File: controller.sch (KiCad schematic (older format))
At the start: 29 parts, among them Q1 Q_PMOS_SGD, Q2 Q_PMOS_SGD, SW1 L1, SW2 L2, SW3 Select, SW4 Start, SW5 R2, SW6 R1, U4 dpad-cross-trace, U5 ProMicro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

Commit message: Add SMD dome switch footprint.
Link diode, dome switch, and pro micro footprints to their symbols. Add
the pro micro subdirectory footprint library to the library list.
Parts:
- D1, D10, D11, D12, D13, D14, D15, D16, D2, D3, D4, D5, D6, D7, D8, D9: footprint (none) -> Diode_THT:D_DO-35_SOD27_P7.62mm_Horizontal
- SW3, SW4: footprint (none) -> rpi-shell-v1-switches:SW_SMD_Dome_TL3312NF-160Q
- U5: footprint (none) -> kicad-pro-micro:ProMicro
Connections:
- wire segments 109 -> 97
- no-connect marks 10 -> 22
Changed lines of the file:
@@
 F 0 "D1" V 2004 1730 50  0000 L CNN
 F 1 "D_Schottky" V 2095 1730 50  0000 L CNN
-F 2 "" H 2050 1650 50  0001 C CNN
+F 2 "Diode_THT:D_DO-35_SOD27_P7.62mm_Horizontal" H 2050 1650 50  0001 C CNN
 F 3 "~" H 2050 1650 50  0001 C CNN
 	1    2050 1650
@@
 F 0 "SW3" H 3500 1585 50  0000 C CNN
 F 1 "Select" H 3500 1494 50  0000 C CNN
-F 2 "" H 3500 1500 50  0001 C CNN
+F 2 "rpi-shell-v1-switches:SW_SMD_Dome_TL3312NF-160Q" H 3500 1500 50  0001 C CNN
 F 3 "http://www.apem.com/int/index.php?controller=attachment&id_attachment=1371" H 3500 1500 50  0001 C CNN
 	1    3500 1200
@@
 F 0 "SW4" H 8150 1685 50  0000 C CNN
 F 1 "Start" H 8150 1594 50  0000 C CNN
-F 2 "" H 8150 1600 50  0001 C CNN
+F 2 "rpi-shell-v1-switches:SW_SMD_Dome_TL3312NF-160Q" H 8150 1600 50  0001 C CNN
 F 3 "http://www.apem.com/int/index.php?controller=attachment&id_attachment=1371" H 8150 1600 50  0001 C CNN
 	1    8150 1300
@@
 F 0 "U5" H 5850 4887 60  0000 C CNN
 F 1 "ProMicro" H 5850 4781 60  0000 C CNN
-F 2 "" H 5950 2800 60  0000 C CNN
+F 2 "kicad-pro-micro:ProMicro" H 5950 2800 60  0001 C CNN
 F 3 "" H 5950 2800 60  0000 C CNN
 	1    5850 3850
@@
 	1500 1200 1500 1350
 Wire Wire Line
-	1650 1100 1650 1200
-Connection ~ 1650 1200
-Wire Wire Line
-	2500 1100 2500 1200
-Wire Wire Line
 	2500 1200 2500 1350
 Wire Wire Line
 	2500 1350 1500 1350
-Connection ~ 2500 1200
-Wire Wire Line
-	3300 1100 3300 1200
 Wire Wire Line
 	3300 1200 3300 1350
 Wire Wire Line
 	3300 1350 2500 1350
-Connection ~ 3300 1200
 Connection ~ 2500 1350
-Wire Wire Line
-	3700 1100 3700 1200
-Wire Wire Line
-	2900 1100 2900 1200
-Wire Wire Line
-	2050 1100 2050 1200
 $Comp
 L Device:D_Schottky D2
@@
 F 0 "D2" V 2854 1730 50  0000 L CNN
 F 1 "D_Schottky" V 2945 1730 50  0000 L CNN
-F 2 "" H 2900 1650 50  0001 C CNN
+F 2 "Diode_THT:D_DO-35_SOD27_P7.62mm_Horizontal" H 2900 1650 50  0001 C CNN
 F 3 "~" H 2900 1650 50  0001 C CNN
 	1    2900 1650
@@
 F 0 "D3" V 3654 1730 50  0000 L CNN
 F 1 "D_Schottky" V 3745 1730 50  0000 L CNN
-F 2 "" H 3700 1650 50  0001 C CNN
+F 2 "Diode_THT:D_DO-35_SOD27_P7.62mm_Horizontal" H 3700 1650 50  0001 C CNN
 F 3 "~" H 3700 1650 50  0001 C CNN
 	1    3700 1650
@@
 Wire Wire Line
 	3700 1200 3700 1500
-Connection ~ 3700 1200
 Wire Wire Line
 	2900 1200 2900 1500
-Connection ~ 2900 1200
 Wire Wire Line
 	2050 1200 2050 1500
-Connection ~ 2050 1200
 Wire Wire Line
 	3300 1350 4300 1350
@@
 F 0 "D14" V 7904 1730 50  0000 L CNN
 F 1 "D_Schottky" V 7995 1730 50  0000 L CNN
-F 2 "" H 7950 1650 50  0001 C CNN
+F 2 "Diode_THT:D_DO-35_SOD27_P7.62mm_Horizontal" H 7950 1650 50  0001 C CNN
 F 3 "~" H 7950 1650 50  0001 C CNN
 	1    7950 1650
@@
 F 0 "D15" V 8654 1730 50  0000 L CNN
 F 1 "D_Schottky" V 8745 1730 50  0000 L CNN
-F 2 "" H 8700 1650 50  0001 C CNN
+F 2 "Diode_THT:D_DO-35_SOD27_P7.62mm_Horizontal" H 8700 1650 50  0001 C CNN
 F 3 "~" H 8700 1650 50  0001 C CNN
 	1    8700 1650
@@
 F 0 "D16" V 9404 1730 50  0000 L CNN
 F 1 "D_Schottky" V 9495 1730 50  0000 L CNN
-F 2 "" H 9450 1650 50  0001 C CNN
+F 2 "Diode_THT:D_DO-35_SOD27_P7.62mm_Horizontal" H 9450 1650 50  0001 C CNN
 F 3 "~" H 9450 1650 50  0001 C CNN
 	1    9450 1650
@@
 $EndComp
 Wire Wire Line
-	7950 1200 7950 1300
-Wire Wire Line
 	7950 1300 7950 1500
-Connection ~ 7950 1300
 Wire Wire Line
 	8700 1300 8700 1500
 Wire Wire Line
-	8700 1200 8700 1300
-Connection ~ 8700 1300
-Wire Wire Line
-	9450 1200 9450 1300
-Wire Wire Line
-	9450 1300 9450 1500
-Connection ~ 9450 1300
-Wire Wire Line
 	7750 4100 6550 4100
 Wire Wire Line
@@
 	7750 3750 7450 3750
 Wire Wire Line
-	9850 1400 9850 1300
-Wire Wire Line
-	9850 1200 9850 1300
-Connection ~ 9850 1300
-Wire Wire Line
-	9100 1200 9100 1300
-Wire Wire Line
 	9100 1300 9100 1400
-Connection ~ 9100 1300
 Connection ~ 9100 1400
 Wire Wire Line
 	9100 1400 9850 1400
 Wire Wire Line
-	8350 1200 8350 1300
-Wire Wire Line
 	8350 1300 8350 1400
-Connection ~ 8350 1300
 Connection ~ 8350 1400
 Wire Wire Line
@@
 Wire Wire Line
 	4300 3600 4000 3600
-$Comp
-L Switch:SW_MEC_5E SW6
-U 1 1 60680BB6
-P 9650 1300
-F 0 "SW6" H 9650 1685 50  0000 C CNN
-F 1 "R1" H 9650 1594 50  0000 C CNN
-F 2 "" H 9650 1600 50  0001 C CNN
-F 3 "http://www.apem.com/int/index.php?controller=attachment&id_attachment=1371" H 9650 1600 50  0001 C CNN
-	1    9650 1300
-	1    0    0    -1
-$EndComp
 Wire Wire Line
 	3650 4400 6800 4400
@@
 F 0 "D4" V 4046 3170 50  0000 R CNN
 F 1 "D_Schottky" V 3955 3170 50  0000 R CNN
-F 2 "" H 4000 3250 50  0001 C CNN
+F 2 "Diode_THT:D_DO-35_SOD27_P7.62mm_Horizontal" H 4000 3250 50  0001 C CNN
 F 3 "~" H 4000 3250 50  0001 C CNN
 	1    4000 3250
@@
 F 0 "D13" V 7796 3420 50  0000 R CNN
 F 1 "D_Schottky" V 7705 3420 50  0000 R CNN
-F 2 "" H 7750 3500 50  0001 C CNN
+F 2 "Diode_THT:D_DO-35_SOD27_P7.62mm_Horizontal" H 7750 3500 50  0001 C CNN
 F 3 "~" H 7750 3500 50  0001 C CNN
 	1    7750 3500
@@
 F 0 "D10" H 6750 4933 50  0000 C CNN
 F 1 "D_Schottky" H 6750 5024 50  0000 C CNN
-F 2 "" H 6750 5150 50  0001 C CNN
+F 2 "Diode_THT:D_DO-35_SOD27_P7.62mm_Horizontal" H 6750 5150 50  0001 C CNN
 F 3 "~" H 6750 5150 50  0001 C CNN
 	1    6750 5150
@@
 F 0 "D11" H 6750 5633 50  0000 C CNN
 F 1 "D_Schottky" H 6750 5724 50  0000 C CNN
-F 2 "" H 6750 5850 50  0001 C CNN
+F 2 "Diode_THT:D_DO-35_SOD27_P7.62mm_Horizontal" H 6750 5850 50  0001 C CNN
 F 3 "~" H 6750 5850 50  0001 C CNN
 	1    6750 5850
@@
 F 0 "D12" H 6750 5933 50  0000 C CNN
 F 1 "D_Schottky" H 6750 6024 50  0000 C CNN
-F 2 "" H 6750 6150 50  0001 C CNN
+F 2 "Diode_THT:D_DO-35_SOD27_P7.62mm_Horizontal" H 6750 6150 50  0001 C CNN
 F 3 "~" H 6750 6150 50  0001 C CNN
 	1    6750 6150
@@
 F 0 "D5" H 4650 5217 50  0000 C CNN
 F 1 "D_Schottky" H 4650 5126 50  0000 C CNN
-F 2 "" H 4650 5000 50  0001 C CNN
+F 2 "Diode_THT:D_DO-35_SOD27_P7.62mm_Horizontal" H 4650 5000 50  0001 C CNN
 F 3 "~" H 4650 5000 50  0001 C CNN
 	1    4650 5000
@@
 F 0 "D6" H 4650 5467 50  0000 C CNN
 F 1 "D_Schottky" H 4650 5376 50  0000 C CNN
-F 2 "" H 4650 5250 50  0001 C CNN
+F 2 "Diode_THT:D_DO-35_SOD27_P7.62mm_Horizontal" H 4650 5250 50  0001 C CNN
 F 3 "~" H 4650 5250 50  0001 C CNN
 	1    4650 5250
@@
 F 0 "D7" H 4650 5867 50  0000 C CNN
 F 1 "D_Schottky" H 4650 5776 50  0000 C CNN
-F 2 "" H 4650 5650 50  0001 C CNN
+F 2 "Diode_THT:D_DO-35_SOD27_P7.62mm_Horizontal" H 4650 5650 50  0001 C CNN
 F 3 "~" H 4650 5650 50  0001 C CNN
 	1    4650 5650
@@
 F 0 "D8" H 4650 6067 50  0000 C CNN
 F 1 "D_Schottky" H 4650 5976 50  0000 C CNN
-F 2 "" H 4650 5850 50  0001 C CNN
+F 2 "Diode_THT:D_DO-35_SOD27_P7.62mm_Horizontal" H 4650 5850 50  0001 C CNN
 F 3 "~" H 4650 5850 50  0001 C CNN
 	1    4650 5850
@@
 F 0 "D9" H 6750 4633 50  0000 C CNN
 F 1 "D_Schottky" H 6750 4724 50  0000 C CNN
-F 2 "" H 6750 4850 50  0001 C CNN
+F 2 "Diode_THT:D_DO-35_SOD27_P7.62mm_Horizontal" H 6750 4850 50  0001 C CNN
 F 3 "~" H 6750 4850 50  0001 C CNN
 	1    6750 4850
@@
 Wire Wire Line
 	8400 3050 8050 3050
+NoConn ~ 1650 1100
+NoConn ~ 2050 1100
+NoConn ~ 2500 1100
+NoConn ~ 2900 1100
+NoConn ~ 3300 1100
+NoConn ~ 3700 1100
+Wire Wire Line
+	9850 1400 9850 1300
+Wire Wire Line
+	9450 1300 9450 1500
+$Comp
+L Switch:SW_MEC_5E SW6
+U 1 1 60680BB6
+P 9650 1300
+F 0 "SW6" H 9650 1685 50  0000 C CNN
+F 1 "R1" H 9650 1594 50  0000 C CNN
+F 2 "" H 9650 1600 50  0001 C CNN
+F 3 "http://www.apem.com/int/index.php?controller=attachment&id_attachment=1371" H 9650 1600 50  0001 C CNN
+	1    9650 1300
+	1    0    0    -1
+$EndComp
+NoConn ~ 9850 1200
+NoConn ~ 9450 1200
+NoConn ~ 9100 1200
+NoConn ~ 8700 1200
+NoConn ~ 8350 1200
+NoConn ~ 7950 1200
 Wire Bus Line
 	5850 2100 9900 2100

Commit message: Add P channel mosfet footprint.
The footprint was modified from the TL2104N3-G mosfet footprint off of
SnapEDA to match the TO-92 packaging dimensions.
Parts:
- Q1, Q2: footprint (none) -> rpi-shell-v1-mosfets:TO127P254X732-3
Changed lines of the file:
@@
 F 0 "Q1" H 4105 2796 50  0000 L CNN
 F 1 "Q_PMOS_SGD" H 4105 2705 50  0000 L CNN
-F 2 "" H 4100 2850 50  0001 C CNN
+F 2 "rpi-shell-v1-mosfets:TO127P254X732-3" H 4100 2850 50  0001 C CNN
 F 3 "~" H 3900 2750 50  0001 C CNN
 	1    3900 2750
@@
 F 0 "Q2" H 8055 3004 50  0000 L CNN
 F 1 "Q_PMOS_SGD" H 8055 3095 50  0000 L CNN
-F 2 "" H 8050 3150 50  0001 C CNN
+F 2 "rpi-shell-v1-mosfets:TO127P254X732-3" H 8050 3150 50  0001 C CNN
 F 3 "~" H 7850 3050 50  0001 C CNN
 	1    7850 3050

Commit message: Add ProMicro socket and trimpot footprints.
Create pro micro socket from the kicad-pro-micro footprint and 2 1x12
female header pin vertical footprints. Turns out the kicad-pro-micro
footprint does not have the same measurements as the actual Arduino Pro
Micro I have, so I had to modify it. Will probably use this footprint
without the pin header in the future.

Get Bourns 3362P trimpot from SnapEDA and make some slight
modifications.
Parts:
- U5: footprint kicad-pro-micro:ProMicro -> rpi-shell-v1-sockets:pro-micro-pin-header-socket
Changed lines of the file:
@@
 F 0 "U5" H 5850 4887 60  0000 C CNN
 F 1 "ProMicro" H 5850 4781 60  0000 C CNN
-F 2 "kicad-pro-micro:ProMicro" H 5950 2800 60  0001 C CNN
+F 2 "rpi-shell-v1-sockets:pro-micro-pin-header-socket" H 5950 2800 60  0001 C CNN
 F 3 "" H 5950 2800 60  0000 C CNN
 	1    5850 3850

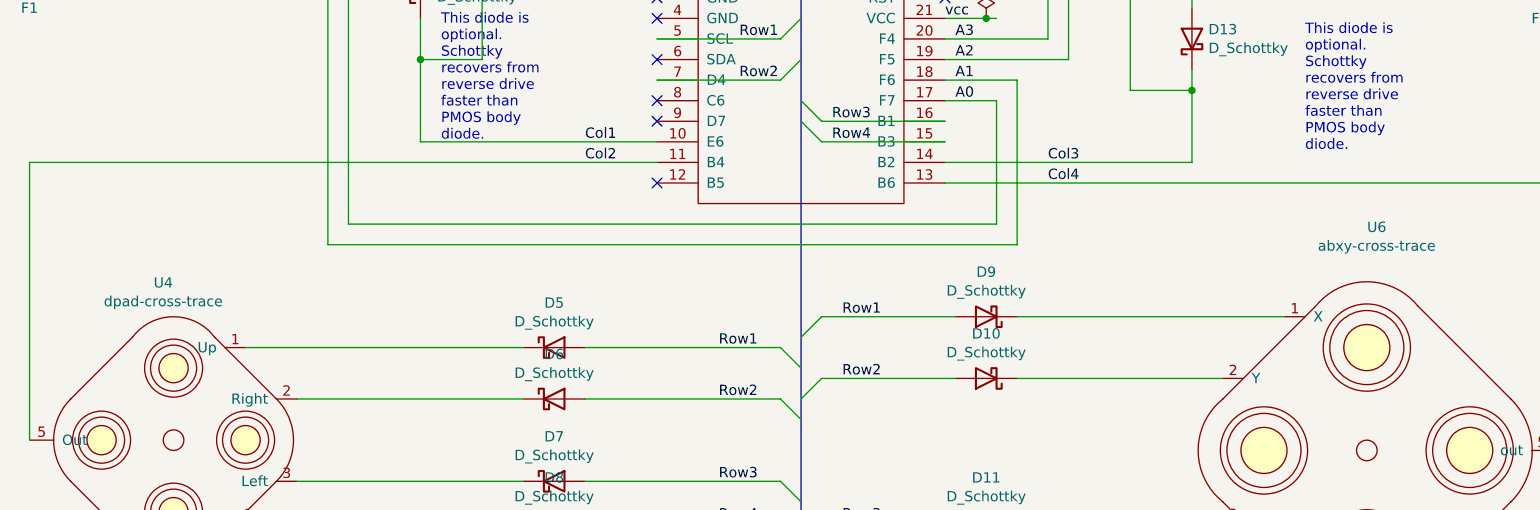
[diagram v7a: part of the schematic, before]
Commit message: Add side-actuated tactile switch footprint.
Made MJTP1236 footprint using datasheet reference in FreeCAD. Imported
to KiCAD using StepUp. Couldn't figure out how to name the through hole
layer properly so I used SMD pads and manually converted them to through
holes inside KiCAD.
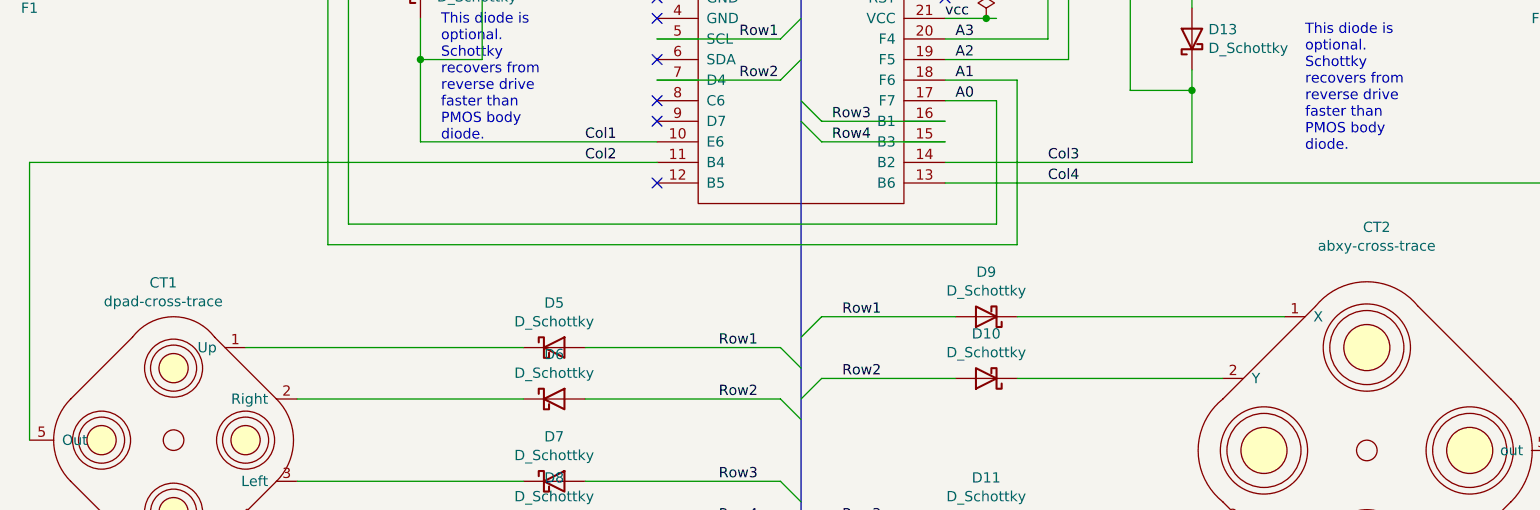
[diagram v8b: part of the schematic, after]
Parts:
- SW1, SW2, SW5, SW6: footprint (none) -> rpi-shell-v1-switches:MJTP1236
- renumbered U4 to CT1, U6 to CT2
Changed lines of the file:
@@
 F 0 "SW1" H 1850 1585 50  0000 C CNN
 F 1 "L1" H 1850 1494 50  0000 C CNN
-F 2 "" H 1850 1500 50  0001 C CNN
+F 2 "rpi-shell-v1-switches:MJTP1236" H 1850 1500 50  0001 C CNN
 F 3 "http://www.apem.com/int/index.php?controller=attachment&id_attachment=1371" H 1850 1500 50  0001 C CNN
 	1    1850 1200
@@
 F 0 "SW2" H 2700 1585 50  0000 C CNN
 F 1 "L2" H 2700 1494 50  0000 C CNN
-F 2 "" H 2700 1500 50  0001 C CNN
+F 2 "rpi-shell-v1-switches:MJTP1236" H 2700 1500 50  0001 C CNN
 F 3 "http://www.apem.com/int/index.php?controller=attachment&id_attachment=1371" H 2700 1500 50  0001 C CNN
 	1    2700 1200
@@
 F 0 "SW5" H 8900 1685 50  0000 C CNN
 F 1 "R2" H 8900 1594 50  0000 C CNN
-F 2 "" H 8900 1600 50  0001 C CNN
+F 2 "rpi-shell-v1-switches:MJTP1236" H 8900 1600 50  0001 C CNN
 F 3 "http://www.apem.com/int/index.php?controller=attachment&id_attachment=1371" H 8900 1600 50  0001 C CNN
 	1    8900 1300
@@
 Col4
 $Comp
-L rpi-shell:dpad-cross-trace U4
+L rpi-shell:dpad-cross-trace CT1
 U 1 1 60680C54
 P 2800 5450
-F 0 "U4" H 2750 6215 50  0000 C CNN
+F 0 "CT1" H 2750 6215 50  0000 C CNN
 F 1 "dpad-cross-trace" H 2750 6124 50  0000 C CNN
 F 2 "" H 2800 4400 50  0001 C CNN
@@
 $EndComp
 $Comp
-L rpi-shell:abxy-cross-trace U6
+L rpi-shell:abxy-cross-trace CT2
 U 1 1 60680C6A
 P 8600 5500
-F 0 "U6" H 8648 6585 50  0000 C CNN
+F 0 "CT2" H 8648 6585 50  0000 C CNN
 F 1 "abxy-cross-trace" H 8648 6494 50  0000 C CNN
 F 2 "" H 8600 5500 50  0001 C CNN
@@
 F 0 "SW6" H 9650 1685 50  0000 C CNN
 F 1 "R1" H 9650 1594 50  0000 C CNN
-F 2 "" H 9650 1600 50  0001 C CNN
+F 2 "rpi-shell-v1-switches:MJTP1236" H 9650 1600 50  0001 C CNN
 F 3 "http://www.apem.com/int/index.php?controller=attachment&id_attachment=1371" H 9650 1600 50  0001 C CNN
 	1    9650 1300
